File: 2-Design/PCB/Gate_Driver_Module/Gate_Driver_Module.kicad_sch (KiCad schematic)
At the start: 8 parts, among them U1 ROE-0512S, U2 LTV-817, U3 TC4421

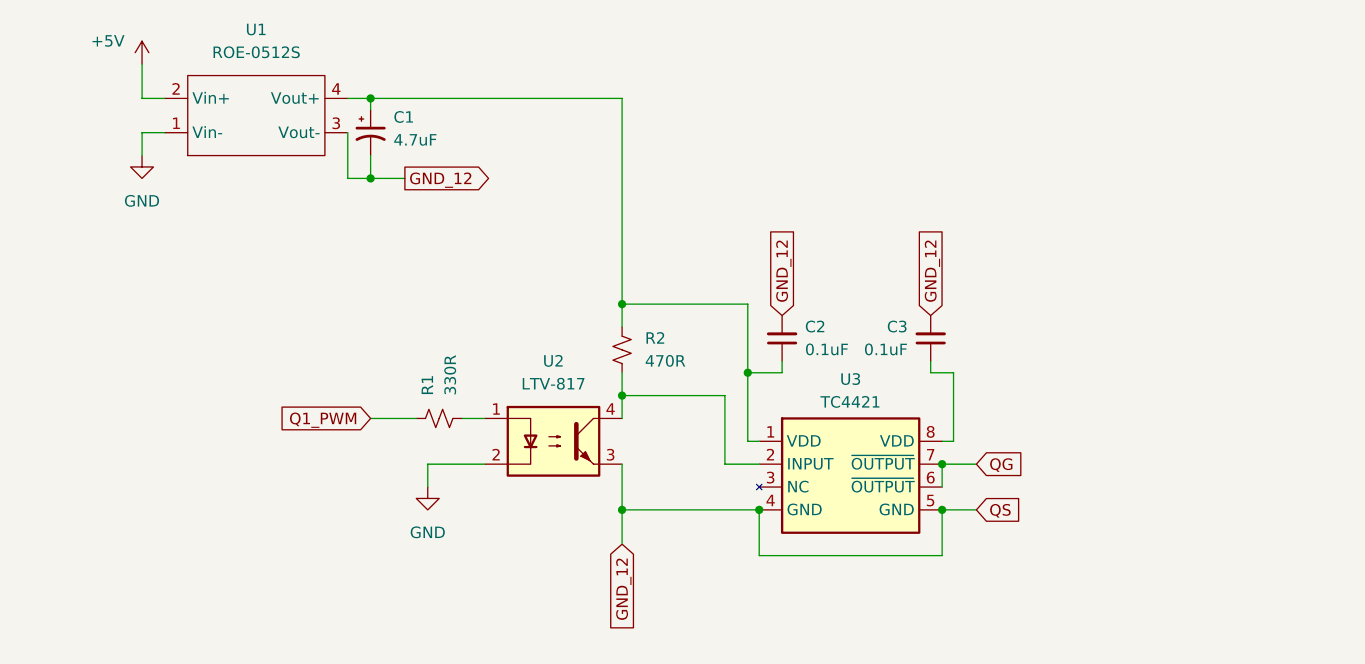
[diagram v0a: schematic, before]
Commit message: Gate Driver Module placements somewhat ready, to be drawn
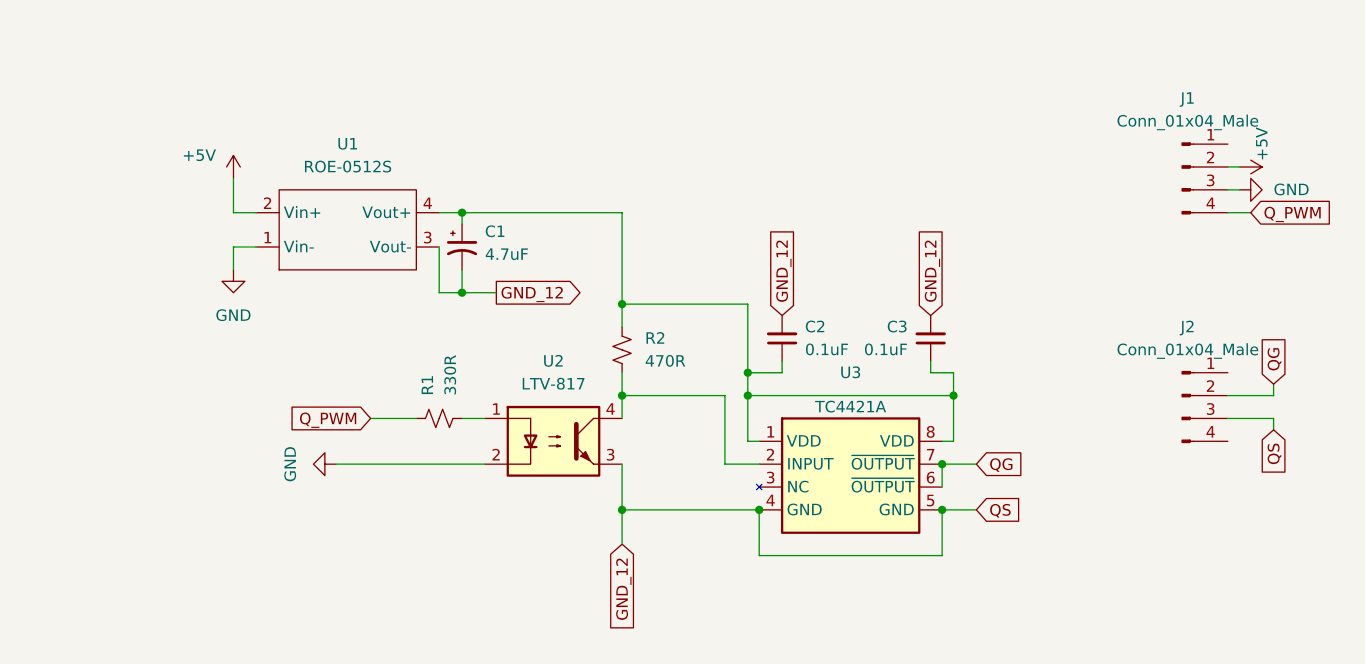
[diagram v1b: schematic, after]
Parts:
- added J1, J2: Conn_01x04_Male, Connector_PinHeader_2.54mm:PinHeader_1x04_P2.54mm_Vertical, symbol Connector:Conn_01x04_Male
- C1: footprint Capacitor_SMD:C_0805_2012Metric_Pad1.18x1.45mm_HandSolder -> Capacitor_SMD:CP_Elec_4x5.4
- U3: value TC4421 -> TC4421A
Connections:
- net +5V: now also J1.2 (Pin_2)
- net GND: now also J1.3 (Pin_3)
- net GND_12: now also J2.3 (Pin_3)
- net QG: now also J2.2 (Pin_2)
- net at C1.1, C2.1, R2.2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: now also C3.1, U3.8 (VDD)
- net Q1_PWM renamed Q_PWM
- net Q_PWM: now also J1.4 (Pin_4)
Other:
- moved on the sheet: C1, U1

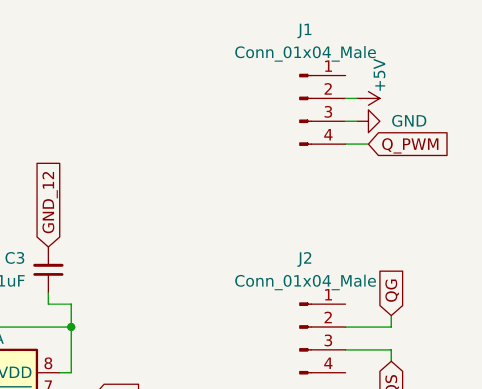
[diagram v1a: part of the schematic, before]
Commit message: Gate Driver Module placements are not somewhat ready, but it takes time for isik to learn
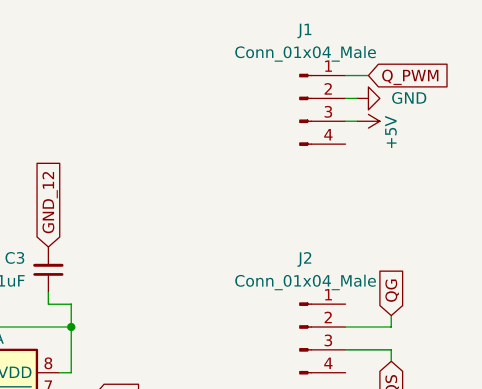
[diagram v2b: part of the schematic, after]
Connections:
- net +5V: now also J1.3 (Pin_3); no longer J1.2 (Pin_2)
- net GND: now also J1.2 (Pin_2); no longer J1.3 (Pin_3)
- net Q_PWM: now also J1.1 (Pin_1); no longer J1.4 (Pin_4)
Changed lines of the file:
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@@
+    (stroke (width 0) (type default) (color 0 0 0 0))
+  )
+  (wire (pts (xy 184.15 59.69) (xy 182.88 59.69))
     (stroke (width 0) (type default) (color 0 0 0 0))
   )
@@
     (stroke (width 0) (type default) (color 0 0 0 0))
   )
-  (wire (pts (xy 184.15 57.15) (xy 182.88 57.15))
+  (wire (pts (xy 182.88 54.61) (xy 185.42 54.61))
     (stroke (width 0) (type default) (color 0 0 0 0))
   )
@@
     (stroke (width 0) (type default) (color 0 0 0 0))
   )
-  (wire (pts (xy 182.88 59.69) (xy 184.15 59.69))
-    (stroke (width 0) (type default) (color 0 0 0 0))
-  )
   (wire (pts (xy 152.4 80.01) (xy 149.86 80.01))
     (stroke (width 0) (type default) (color 0 0 0 0))
@@
     (stroke (width 0) (type default) (color 0 0 0 0))
   )
+  (wire (pts (xy 182.88 57.15) (xy 184.15 57.15))
+    (stroke (width 0) (type default) (color 0 0 0 0))
+  )
   (wire (pts (xy 127 82.55) (xy 127 90.17))
     (stroke (width 0) (type default) (color 0 0 0 0))
@@
   )
   (wire (pts (xy 97.79 71.12) (xy 101.6 71.12))
-    (stroke (width 0) (type default) (color 0 0 0 0))
-  )
-  (wire (pts (xy 182.88 62.23) (xy 185.42 62.23))
     (stroke (width 0) (type default) (color 0 0 0 0))
   )
@@
     )
   )
-  (global_label "Q_PWM" (shape input) (at 185.42 62.23 0) (fields_autoplaced)
-    (effects (font (size 1.27 1.27)) (justify left))
-    (property "Intersheet References" "${INTERSHEET_REFS}" (id 0) (at 194.3041 62.1506 0)
-      (effects (font (size 1.27 1.27)) (justify left) hide)
-    )
-  )
   (global_label "QG" (shape input) (at 187.96 81.28 90) (fields_autoplaced)
     (effects (font (size 1.27 1.27)) (justify left))
@@
     (effects (font (size 1.27 1.27)) (justify left))
     (property "Intersheet References" "${INTERSHEET_REFS}" (id 0) (at 111.2702 71.1994 0)
+      (effects (font (size 1.27 1.27)) (justify left) hide)
+    )
+  )
+  (global_label "Q_PWM" (shape input) (at 185.42 54.61 0) (fields_autoplaced)
+    (effects (font (size 1.27 1.27)) (justify left))
+    (property "Intersheet References" "${INTERSHEET_REFS}" (id 0) (at 194.3041 54.5306 0)
       (effects (font (size 1.27 1.27)) (justify left) hide)
     )
@@
     (pin "2")
   )
+  (symbol (lib_id "power:+5V") (at 184.15 59.69 270) (unit 1)
+    (in_bom yes) (on_board yes)
+    (property "Reference" "#PWR0105" (id 0) (at 180.34 59.69 0)
+      (effects (font (size 1.27 1.27)) hide)
+    )
+    (property "Value" "+5V" (id 1) (at 187.96 60.96 0))
+    (property "Footprint" "" (id 2) (at 184.15 59.69 0)
+      (effects (font (size 1.27 1.27)) hide)
+    )
+    (property "Datasheet" "" (id 3) (at 184.15 59.69 0)
+      (effects (font (size 1.27 1.27)) hide)
+    )
+    (pin "1")
+  )
   (symbol (lib_id "ee463_symbol_library:ROE-0512S") (at 85.09 64.77 0) (mirror x) (unit 1)
     (in_bom yes) (on_board yes) (fields_autoplaced)
@@
     (pin "4")
   )
-  (symbol (lib_id "power:+5V") (at 184.15 57.15 270) (unit 1)
-    (in_bom yes) (on_board yes)
-    (property "Reference" "#PWR0104" (id 0) (at 180.34 57.15 0)
-      (effects (font (size 1.27 1.27)) hide)
-    )
-    (property "Value" "+5V" (id 1) (at 186.69 54.61 0))
-    (property "Footprint" "" (id 2) (at 184.15 57.15 0)
-      (effects (font (size 1.27 1.27)) hide)
-    )
-    (property "Datasheet" "" (id 3) (at 184.15 57.15 0)
-      (effects (font (size 1.27 1.27)) hide)
-    )
-    (pin "1")
-  )
   (symbol (lib_id "power:+5V") (at 72.39 58.42 0) (unit 1)
     (in_bom yes) (on_board yes)
@@
     )
     (property "Datasheet" "" (id 3) (at 72.39 58.42 0)
-      (effects (font (size 1.27 1.27)) hide)
-    )
-    (pin "1")
-  )
-  (symbol (lib_id "power:GND") (at 184.15 59.69 90) (unit 1)
-    (in_bom yes) (on_board yes) (fields_autoplaced)
-    (property "Reference" "#PWR0105" (id 0) (at 190.5 59.69 0)
-      (effects (font (size 1.27 1.27)) hide)
-    )
-    (property "Value" "GND" (id 1) (at 187.96 59.6899 90)
-      (effects (font (size 1.27 1.27)) (justify right))
-    )
-    (property "Footprint" "" (id 2) (at 184.15 59.69 0)
-      (effects (font (size 1.27 1.27)) hide)
-    )
-    (property "Datasheet" "" (id 3) (at 184.15 59.69 0)
       (effects (font (size 1.27 1.27)) hide)
     )
@@
     (pin "1")
   )
+  (symbol (lib_id "power:GND") (at 184.15 57.15 90) (unit 1)
+    (in_bom yes) (on_board yes) (fields_autoplaced)
+    (property "Reference" "#PWR?" (id 0) (at 190.5 57.15 0)
+      (effects (font (size 1.27 1.27)) hide)
+    )
+    (property "Value" "GND" (id 1) (at 187.96 57.1499 90)
+      (effects (font (size 1.27 1.27)) (justify right))
+    )
+    (property "Footprint" "" (id 2) (at 184.15 57.15 0)
+      (effects (font (size 1.27 1.27)) hide)
+    )
+    (property "Datasheet" "" (id 3) (at 184.15 57.15 0)
+      (effects (font (size 1.27 1.27)) hide)
+    )
+    (pin "1")
+  )
   (symbol (lib_id "Connector:Conn_01x04_Male") (at 177.8 57.15 0) (unit 1)
     (in_bom yes) (on_board yes) (fields_autoplaced)
@@
       (reference "#PWR0103") (unit 1) (value "GND") (footprint "")
     )
-    (path "/909a5f4c-be4c-4a21-bdbf-ea647c4dfad1"
-      (reference "#PWR0104") (unit 1) (value "+5V") (footprint "")
-    )
-    (path "/9cd18db6-3c5d-4ffe-9b82-0fb94a74c918"
-      (reference "#PWR0105") (unit 1) (value "GND") (footprint "")
+    (path "/32fe396f-30eb-4ab2-951d-69250d85cd3f"
+      (reference "#PWR0105") (unit 1) (value "+5V") (footprint "")
+    )
+    (path "/dc665fed-2ed1-462c-8830-d3267e225455"
+      (reference "#PWR?") (unit 1) (value "GND") (footprint "")
     )
     (path "/7d5e55a6-9259-481f-a970-5a6c82e212d5"

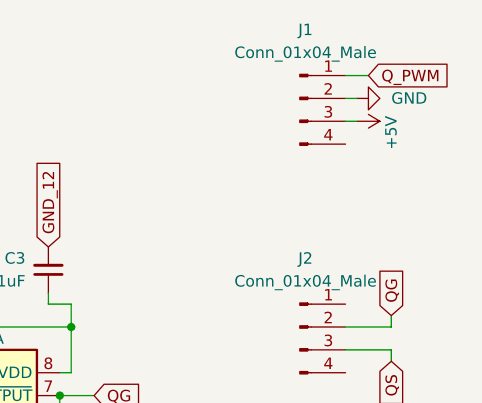
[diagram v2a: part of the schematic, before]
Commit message: Gate Driver Module v1 completed, minor polishing to be done
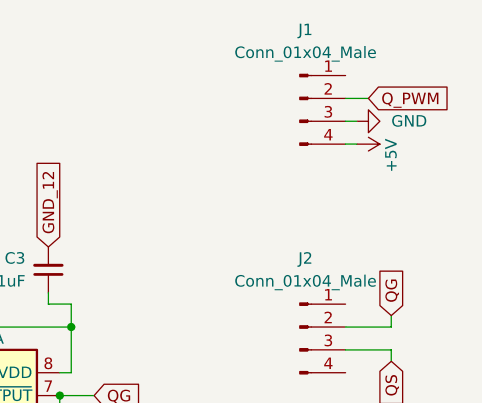
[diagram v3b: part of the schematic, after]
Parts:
- U2: footprint Package_DIP:DIP-4_W7.62mm -> Package_DIP:SMDIP-4_W7.62mm
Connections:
- net +5V: now also J1.4 (Pin_4); no longer J1.3 (Pin_3)
- net GND: now also J1.3 (Pin_3); no longer J1.2 (Pin_2)
- net Q_PWM: now also J1.2 (Pin_2); no longer J1.1 (Pin_1)
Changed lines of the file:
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@@
-    (stroke (width 0) (type default) (color 0 0 0 0))
-  )
-  (wire (pts (xy 184.15 59.69) (xy 182.88 59.69))
     (stroke (width 0) (type default) (color 0 0 0 0))
   )
@@
     (stroke (width 0) (type default) (color 0 0 0 0))
   )
+  (wire (pts (xy 184.15 62.23) (xy 182.88 62.23))
+    (stroke (width 0) (type default) (color 0 0 0 0))
+  )
   (wire (pts (xy 97.79 62.23) (xy 97.79 63.5))
     (stroke (width 0) (type default) (color 0 0 0 0))
@@
     (stroke (width 0) (type default) (color 0 0 0 0))
   )
+  (wire (pts (xy 182.88 57.15) (xy 185.42 57.15))
+    (stroke (width 0) (type default) (color 0 0 0 0))
+  )
   (wire (pts (xy 72.39 58.42) (xy 72.39 62.23))
     (stroke (width 0) (type default) (color 0 0 0 0))
@@
     (stroke (width 0) (type default) (color 0 0 0 0))
   )
+  (wire (pts (xy 182.88 59.69) (xy 184.15 59.69))
+    (stroke (width 0) (type default) (color 0 0 0 0))
+  )
   (wire (pts (xy 115.57 82.55) (xy 115.57 85.09))
     (stroke (width 0) (type default) (color 0 0 0 0))
@@
     (stroke (width 0) (type default) (color 0 0 0 0))
   )
-  (wire (pts (xy 182.88 54.61) (xy 185.42 54.61))
-    (stroke (width 0) (type default) (color 0 0 0 0))
-  )
   (wire (pts (xy 130.81 87.63) (xy 129.54 87.63))
     (stroke (width 0) (type default) (color 0 0 0 0))
@@
     (stroke (width 0) (type default) (color 0 0 0 0))
   )
-  (wire (pts (xy 182.88 57.15) (xy 184.15 57.15))
-    (stroke (width 0) (type default) (color 0 0 0 0))
-  )
   (wire (pts (xy 127 82.55) (xy 127 90.17))
     (stroke (width 0) (type default) (color 0 0 0 0))
@@
   (wire (pts (xy 97.79 71.12) (xy 101.6 71.12))
     (stroke (width 0) (type default) (color 0 0 0 0))
+  )
+  (global_label "Q_PWM" (shape input) (at 185.42 57.15 0) (fields_autoplaced)
+    (effects (font (size 1.27 1.27)) (justify left))
+    (property "Intersheet References" "${INTERSHEET_REFS}" (id 0) (at 194.3041 57.0706 0)
+      (effects (font (size 1.27 1.27)) (justify left) hide)
+    )
   )
   (global_label "GND_12" (shape input) (at 115.57 99.06 270) (fields_autoplaced)
@@
     )
   )
-  (global_label "Q_PWM" (shape input) (at 185.42 54.61 0) (fields_autoplaced)
-    (effects (font (size 1.27 1.27)) (justify left))
-    (property "Intersheet References" "${INTERSHEET_REFS}" (id 0) (at 194.3041 54.5306 0)
-      (effects (font (size 1.27 1.27)) (justify left) hide)
-    )
-  )
   (global_label "QG" (shape input) (at 154.94 90.17 0) (fields_autoplaced)
     (effects (font (size 1.27 1.27)) (justify left))
@@
     (pin "2")
   )
-  (symbol (lib_id "power:+5V") (at 184.15 59.69 270) (unit 1)
-    (in_bom yes) (on_board yes)
-    (property "Reference" "#PWR0105" (id 0) (at 180.34 59.69 0)
-      (effects (font (size 1.27 1.27)) hide)
-    )
-    (property "Value" "+5V" (id 1) (at 187.96 60.96 0))
-    (property "Footprint" "" (id 2) (at 184.15 59.69 0)
-      (effects (font (size 1.27 1.27)) hide)
-    )
-    (property "Datasheet" "" (id 3) (at 184.15 59.69 0)
-      (effects (font (size 1.27 1.27)) hide)
-    )
-    (pin "1")
-  )
   (symbol (lib_id "ee463_symbol_library:ROE-0512S") (at 85.09 64.77 0) (mirror x) (unit 1)
     (in_bom yes) (on_board yes) (fields_autoplaced)
@@
     (pin "2")
   )
+  (symbol (lib_id "power:+5V") (at 184.15 62.23 270) (unit 1)
+    (in_bom yes) (on_board yes)
+    (property "Reference" "#PWR0104" (id 0) (at 180.34 62.23 0)
+      (effects (font (size 1.27 1.27)) hide)
+    )
+    (property "Value" "+5V" (id 1) (at 187.96 63.5 0))
+    (property "Footprint" "" (id 2) (at 184.15 62.23 0)
+      (effects (font (size 1.27 1.27)) hide)
+    )
+    (property "Datasheet" "" (id 3) (at 184.15 62.23 0)
+      (effects (font (size 1.27 1.27)) hide)
+    )
+    (pin "1")
+  )
   (symbol (lib_id "Device:C_Small") (at 133.35 76.2 180) (unit 1)
     (in_bom yes) (on_board yes) (fields_autoplaced)
@@
     (property "Reference" "U2" (id 0) (at 107.95 78.74 0))
     (property "Value" "LTV-817" (id 1) (at 107.95 81.28 0))
-    (property "Footprint" "Package_DIP:DIP-4_W7.62mm" (id 2) (at 102.87 92.71 0)
+    (property "Footprint" "Package_DIP:SMDIP-4_W7.62mm" (id 2) (at 102.87 92.71 0)
       (effects (font (size 1.27 1.27) italic) (justify left) hide)
     )
@@
     (pin "1")
   )
-  (symbol (lib_id "power:GND") (at 184.15 57.15 90) (unit 1)
-    (in_bom yes) (on_board yes) (fields_autoplaced)
-    (property "Reference" "#PWR?" (id 0) (at 190.5 57.15 0)
-      (effects (font (size 1.27 1.27)) hide)
-    )
-    (property "Value" "GND" (id 1) (at 187.96 57.1499 90)
-      (effects (font (size 1.27 1.27)) (justify right))
-    )
-    (property "Footprint" "" (id 2) (at 184.15 57.15 0)
-      (effects (font (size 1.27 1.27)) hide)
-    )
-    (property "Datasheet" "" (id 3) (at 184.15 57.15 0)
+  (symbol (lib_id "power:GND") (at 184.15 59.69 90) (unit 1)
+    (in_bom yes) (on_board yes)
+    (property "Reference" "#PWR0105" (id 0) (at 190.5 59.69 0)
+      (effects (font (size 1.27 1.27)) hide)
+    )
+    (property "Value" "GND" (id 1) (at 187.96 59.69 90)
+      (effects (font (size 1.27 1.27)) (justify right))
+    )
+    (property "Footprint" "" (id 2) (at 184.15 59.69 0)
+      (effects (font (size 1.27 1.27)) hide)
+    )
+    (property "Datasheet" "" (id 3) (at 184.15 59.69 0)
       (effects (font (size 1.27 1.27)) hide)
     )
@@
       (reference "#PWR0103") (unit 1) (value "GND") (footprint "")
     )
-    (path "/32fe396f-30eb-4ab2-951d-69250d85cd3f"
-      (reference "#PWR0105") (unit 1) (value "+5V") (footprint "")
-    )
-    (path "/dc665fed-2ed1-462c-8830-d3267e225455"
-      (reference "#PWR?") (unit 1) (value "GND") (footprint "")
+    (path "/6db353c8-ae39-4b79-955a-3904d10f4c31"
+      (reference "#PWR0104") (unit 1) (value "+5V") (footprint "")
+    )
+    (path "/e64de5f4-ff91-40e3-952f-9e9eece738bc"
+      (reference "#PWR0105") (unit 1) (value "GND") (footprint "")
     )
     (path "/7d5e55a6-9259-481f-a970-5a6c82e212d5"
@@
     )
     (path "/8135769e-8054-4464-99f1-f8086d306cff"
-      (reference "U2") (unit 1) (value "LTV-817") (footprint "Package_DIP:DIP-4_W7.62mm")
+      (reference "U2") (unit 1) (value "LTV-817") (footprint "Package_DIP:SMDIP-4_W7.62mm")
     )
     (path "/a41d7a1a-9f1a-44d5-8c5f-c210f6c6d53e"
